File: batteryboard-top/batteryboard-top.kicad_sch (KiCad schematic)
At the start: 6 parts

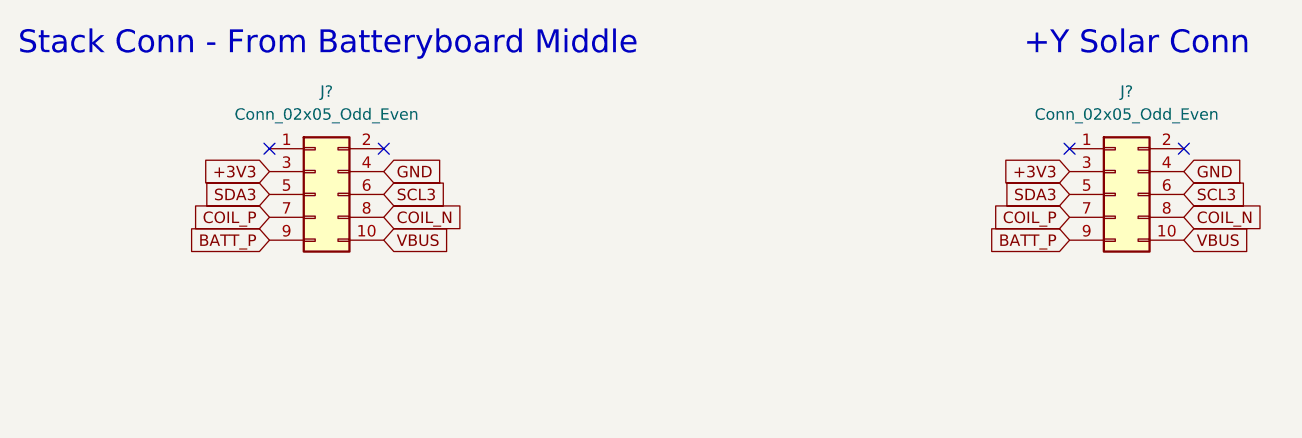
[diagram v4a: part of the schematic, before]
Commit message: Added connectors and traces
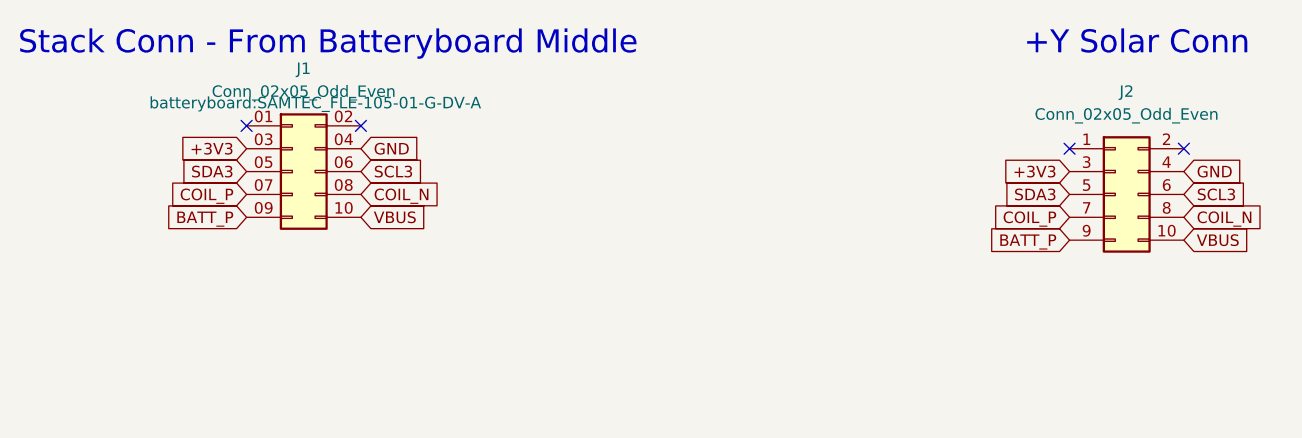
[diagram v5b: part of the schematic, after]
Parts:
- removed J?: Conn_02x05_Odd_Even, symbol Connector_Generic:Conn_02x05_Odd_Even
- added J1: Conn_02x05_Odd_Even, batteryboard:SAMTEC_FLE-105-01-G-DV-A, symbol Connector_Generic:Conn_02x05_Odd_Even
- J2: renamed from J?; footprint (none) -> batteryboard:SAMTEC-FTS-105-01-X-DV
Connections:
- net +3V3: now also J1.03 (Pin_3)
- net BATT_P: now also J1.09 (Pin_9)
- net COIL_N: now also J1.08 (Pin_8)
- net COIL_P: now also J1.07 (Pin_7)
- net GND: now also J1.04 (Pin_4)
- net SCL3: now also J1.06 (Pin_6)
- net SDA3: now also J1.05 (Pin_5)
- net VBUS: now also J1.10 (Pin_10)
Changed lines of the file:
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@@
   (no_connect (at 152.4 38.1))
   (no_connect (at 139.7 38.1))
-  (no_connect (at 63.5 38.1))
-  (no_connect (at 50.8 38.1))
+  (no_connect (at 60.96 35.56))
+  (no_connect (at 48.26 35.56))
   (text "+Y Solar Conn" (at 134.62 27.94 0)
     (effects (font (size 2.54 2.54)) (justify left bottom))
@@
     )
   )
-  (global_label "COIL_N" (shape input) (at 63.5 45.72 0) (fields_autoplaced)
-    (effects (font (size 1.27 1.27)) (justify left))
-    (property "Intersheet References" "${INTERSHEET_REFS}" (id 0) (at 72.4445 45.6406 0)
+  (global_label "COIL_N" (shape input) (at 60.96 43.18 0) (fields_autoplaced)
+    (effects (font (size 1.27 1.27)) (justify left))
+    (property "Intersheet References" "${INTERSHEET_REFS}" (id 0) (at 69.9045 43.1006 0)
       (effects (font (size 1.27 1.27)) (justify left) hide)
     )
@@
     )
   )
-  (global_label "GND" (shape input) (at 63.5 40.64 0) (fields_autoplaced)
-    (effects (font (size 1.27 1.27)) (justify left))
-    (property "Intersheet References" "${INTERSHEET_REFS}" (id 0) (at 69.7836 40.5606 0)
-      (effects (font (size 1.27 1.27)) (justify left) hide)
-    )
-  )
-  (global_label "BATT_P" (shape input) (at 50.8 48.26 180) (fields_autoplaced)
-    (effects (font (size 1.27 1.27)) (justify right))
-    (property "Intersheet References" "${INTERSHEET_REFS}" (id 0) (at 41.8555 48.1806 0)
+  (global_label "GND" (shape input) (at 60.96 38.1 0) (fields_autoplaced)
+    (effects (font (size 1.27 1.27)) (justify left))
+    (property "Intersheet References" "${INTERSHEET_REFS}" (id 0) (at 67.2436 38.0206 0)
+      (effects (font (size 1.27 1.27)) (justify left) hide)
+    )
+  )
+  (global_label "BATT_P" (shape input) (at 48.26 45.72 180) (fields_autoplaced)
+    (effects (font (size 1.27 1.27)) (justify right))
+    (property "Intersheet References" "${INTERSHEET_REFS}" (id 0) (at 39.3155 45.6406 0)
       (effects (font (size 1.27 1.27)) (justify right) hide)
     )
@@
     )
   )
-  (global_label "SCL3" (shape input) (at 63.5 43.18 0) (fields_autoplaced)
-    (effects (font (size 1.27 1.27)) (justify left))
-    (property "Intersheet References" "${INTERSHEET_REFS}" (id 0) (at 70.6302 43.1006 0)
+  (global_label "SCL3" (shape input) (at 60.96 40.64 0) (fields_autoplaced)
+    (effects (font (size 1.27 1.27)) (justify left))
+    (property "Intersheet References" "${INTERSHEET_REFS}" (id 0) (at 68.0902 40.5606 0)
       (effects (font (size 1.27 1.27)) (justify left) hide)
     )
@@
     )
   )
-  (global_label "+3V3" (shape input) (at 50.8 40.64 180) (fields_autoplaced)
-    (effects (font (size 1.27 1.27)) (justify right))
-    (property "Intersheet References" "${INTERSHEET_REFS}" (id 0) (at 43.3069 40.5606 0)
+  (global_label "+3V3" (shape input) (at 48.26 38.1 180) (fields_autoplaced)
+    (effects (font (size 1.27 1.27)) (justify right))
+    (property "Intersheet References" "${INTERSHEET_REFS}" (id 0) (at 40.7669 38.0206 0)
       (effects (font (size 1.27 1.27)) (justify right) hide)
     )
@@
     )
   )
-  (global_label "SDA3" (shape input) (at 50.8 43.18 180) (fields_autoplaced)
-    (effects (font (size 1.27 1.27)) (justify right))
-    (property "Intersheet References" "${INTERSHEET_REFS}" (id 0) (at 43.6093 43.1006 0)
+  (global_label "SDA3" (shape input) (at 48.26 40.64 180) (fields_autoplaced)
+    (effects (font (size 1.27 1.27)) (justify right))
+    (property "Intersheet References" "${INTERSHEET_REFS}" (id 0) (at 41.0693 40.5606 0)
       (effects (font (size 1.27 1.27)) (justify right) hide)
     )
@@
     )
   )
-  (global_label "VBUS" (shape input) (at 63.5 48.26 0) (fields_autoplaced)
-    (effects (font (size 1.27 1.27)) (justify left))
-    (property "Intersheet References" "${INTERSHEET_REFS}" (id 0) (at 70.8117 48.1806 0)
-      (effects (font (size 1.27 1.27)) (justify left) hide)
-    )
-  )
-  (global_label "COIL_P" (shape input) (at 50.8 45.72 180) (fields_autoplaced)
-    (effects (font (size 1.27 1.27)) (justify right))
-    (property "Intersheet References" "${INTERSHEET_REFS}" (id 0) (at 41.9159 45.6406 0)
+  (global_label "VBUS" (shape input) (at 60.96 45.72 0) (fields_autoplaced)
+    (effects (font (size 1.27 1.27)) (justify left))
+    (property "Intersheet References" "${INTERSHEET_REFS}" (id 0) (at 68.2717 45.6406 0)
+      (effects (font (size 1.27 1.27)) (justify left) hide)
+    )
+  )
+  (global_label "COIL_P" (shape input) (at 48.26 43.18 180) (fields_autoplaced)
+    (effects (font (size 1.27 1.27)) (justify right))
+    (property "Intersheet References" "${INTERSHEET_REFS}" (id 0) (at 39.3759 43.1006 0)
       (effects (font (size 1.27 1.27)) (justify right) hide)
     )
@@
     (pin "1")
   )
+  (symbol (lib_name "Conn_02x05_Odd_Even_1") (lib_id "Connector_Generic:Conn_02x05_Odd_Even") (at 53.34 40.64 0) (unit 1)
+    (in_bom yes) (on_board yes) (fields_autoplaced)
+    (property "Reference" "J1" (id 0) (at 54.61 29.21 0))
+    (property "Value" "Conn_02x05_Odd_Even" (id 1) (at 54.61 31.75 0))
+    (property "Footprint" "batteryboard:SAMTEC_FLE-105-01-G-DV-A" (id 2) (at 55.88 33.02 0))
+    (property "Datasheet" "~" (id 3) (at 53.34 40.64 0)
+      (effects (font (size 1.27 1.27)) hide)
+    )
+    (pin "01")
+    (pin "10")
+    (pin "02")
+    (pin "03")
+    (pin "04")
+    (pin "05")
+    (pin "06")
+    (pin "07")
+    (pin "08")
+    (pin "09")
+  )
   (symbol (lib_id "Mechanical:MountingHole_Pad") (at 113.665 82.804 90) (unit 1)
     (in_bom yes) (on_board yes)
@@
     (pin "1")
   )
-  (symbol (lib_id "Connector_Generic:Conn_02x05_Odd_Even") (at 55.88 43.18 0) (unit 1)
+  (symbol (lib_id "Mechanical:MountingHole_Pad") (at 113.665 88.265 90) (unit 1)
+    (in_bom yes) (on_board yes)
+    (property "Reference" "H4" (id 0) (at 132.588 86.233 90))
+    (property "Value" "MountingHole_Pad" (id 1) (at 132.588 88.7699 90))
+    (property "Footprint" "mainboard:MountingHole" (id 2) (at 113.665 88.265 0)
+      (effects (font (size 1.27 1.27)) hide)
+    )
+    (property "Datasheet" "~" (id 3) (at 113.665 88.265 0)
+      (effects (font (size 1.27 1.27)) hide)
+    )
+    (pin "1")
+  )
+  (symbol (lib_id "Mechanical:MountingHole_Pad") (at 96.139 82.804 90) (unit 1)
+    (in_bom yes) (on_board yes)
+    (property "Reference" "H2" (id 0) (at 83.947 80.7751 90))
+    (property "Value" "MountingHole_Pad" (id 1) (at 83.947 83.312 90))
+    (property "Footprint" "mainboard:MountingHole" (id 2) (at 96.139 82.804 0)
+      (effects (font (size 1.27 1.27)) hide)
+    )
+    (property "Datasheet" "~" (id 3) (at 96.139 82.804 0)
+      (effects (font (size 1.27 1.27)) hide)
+    )
+    (pin "1")
+  )
+  (symbol (lib_id "Connector_Generic:Conn_02x05_Odd_Even") (at 144.78 43.18 0) (unit 1)
     (in_bom yes) (on_board yes) (fields_autoplaced)
-    (property "Reference" "J?" (id 0) (at 57.15 31.75 0))
-    (property "Value" "Conn_02x05_Odd_Even" (id 1) (at 57.15 34.29 0))
-    (property "Footprint" "" (id 2) (at 55.88 43.18 0)
-      (effects (font (size 1.27 1.27)) hide)
-    )
-    (property "Datasheet" "~" (id 3) (at 55.88 43.18 0)
+    (property "Reference" "J2" (id 0) (at 146.05 31.75 0))
+    (property "Value" "Conn_02x05_Odd_Even" (id 1) (at 146.05 34.29 0))
+    (property "Footprint" "batteryboard:SAMTEC-FTS-105-01-X-DV" (id 2) (at 144.78 43.18 0)
+      (effects (font (size 1.27 1.27)) hide)
+    )
+    (property "Datasheet" "~" (id 3) (at 144.78 43.18 0)
       (effects (font (size 1.27 1.27)) hide)
     )
@@
     (pin "9")
   )
-  (symbol (lib_id "Mechanical:MountingHole_Pad") (at 113.665 88.265 90) (unit 1)
-    (in_bom yes) (on_board yes)
-    (property "Reference" "H4" (id 0) (at 132.588 86.233 90))
-    (property "Value" "MountingHole_Pad" (id 1) (at 132.588 88.7699 90))
-    (property "Footprint" "mainboard:MountingHole" (id 2) (at 113.665 88.265 0)
-      (effects (font (size 1.27 1.27)) hide)
-    )
-    (property "Datasheet" "~" (id 3) (at 113.665 88.265 0)
-      (effects (font (size 1.27 1.27)) hide)
-    )
-    (pin "1")
-  )
-  (symbol (lib_id "Mechanical:MountingHole_Pad") (at 96.139 82.804 90) (unit 1)
-    (in_bom yes) (on_board yes)
-    (property "Reference" "H2" (id 0) (at 83.947 80.7751 90))
-    (property "Value" "MountingHole_Pad" (id 1) (at 83.947 83.312 90))
-    (property "Footprint" "mainboard:MountingHole" (id 2) (at 96.139 82.804 0)
-      (effects (font (size 1.27 1.27)) hide)
-    )
-    (property "Datasheet" "~" (id 3) (at 96.139 82.804 0)
-      (effects (font (size 1.27 1.27)) hide)
-    )
-    (pin "1")
-  )
-  (symbol (lib_id "Connector_Generic:Conn_02x05_Odd_Even") (at 144.78 43.18 0) (unit 1)
-    (in_bom yes) (on_board yes) (fields_autoplaced)
-    (property "Reference" "J?" (id 0) (at 146.05 31.75 0))
-    (property "Value" "Conn_02x05_Odd_Even" (id 1) (at 146.05 34.29 0))
-    (property "Footprint" "" (id 2) (at 144.78 43.18 0)
-      (effects (font (size 1.27 1.27)) hide)
-    )
-    (property "Datasheet" "~" (id 3) (at 144.78 43.18 0)
-      (effects (font (size 1.27 1.27)) hide)
-    )
-    (pin "1")
-    (pin "10")
-    (pin "2")
-    (pin "3")
-    (pin "4")
-    (pin "5")
-    (pin "6")
-    (pin "7")
-    (pin "8")
-    (pin "9")
-  )
   (symbol (lib_id "power:GND") (at 116.205 82.804 90) (unit 1)
     (in_bom yes) (on_board yes)
@@
       (reference "H4") (unit 1) (value "MountingHole_Pad") (footprint "mainboard:MountingHole")
     )
-    (path "/956f8a88-9acc-4e52-9280-d386fdb26e68"
-      (reference "J?") (unit 1) (value "Conn_02x05_Odd_Even") (footprint "")
+    (path "/7a8c43eb-85f6-4642-ad87-a4fd9f5b5654"
+      (reference "J1") (unit 1) (value "Conn_02x05_Odd_Even") (footprint "batteryboard:SAMTEC_FLE-105-01-G-DV-A")
     )
     (path "/bbe95b8a-8b74-437f-bc35-372bc66b2abb"
-      (reference "J?") (unit 1) (value "Conn_02x05_Odd_Even") (footprint "")
-    )
-  )
+      (reference "J2") (unit 1) (value "Conn_02x05_Odd_Even") (footprint "batteryboard:SAMTEC-FTS-105-01-X-DV")
+    )
+  )

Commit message: Fixes and cleanup
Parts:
- J2: footprint batteryboard:SAMTEC-FTS-105-01-X-DV -> batteryboard:FTS-105-XX-YY-DV-A
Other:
- moved on the sheet: H1, H2, H3, H4, J1, J2

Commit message: Recheck boards and re-export models
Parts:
- J1: value Conn_02x05_Odd_Even -> FLE-105-01-G-DV-A
- J2: value Conn_02x05_Odd_Even -> FLE-105-01-G-DV-A; footprint batteryboard:FTS-105-XX-YY-DV-A -> batteryboard:SAMTEC_FLE-105-01-G-DV-A
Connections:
- net +3V3: now also J1.3 (Pin_3); no longer J1.03 (Pin_3)
- net BATT_P: now also J1.9 (Pin_9); no longer J1.09 (Pin_9)
- net COIL_N: now also J1.8 (Pin_8); no longer J1.08 (Pin_8)
- net COIL_P: now also J1.7 (Pin_7); no longer J1.07 (Pin_7)
- net GND: now also J1.4 (Pin_4); no longer J1.04 (Pin_4)
- net SCL3: now also J1.6 (Pin_6); no longer J1.06 (Pin_6)
- net SDA3: now also J1.5 (Pin_5); no longer J1.05 (Pin_5)
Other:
- moved on the sheet: H1, H2, H3, H4, J1, J2
